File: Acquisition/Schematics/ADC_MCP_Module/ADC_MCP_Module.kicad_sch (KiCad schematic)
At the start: 35 parts, among them J1 Can, J2 AudioJack4_SwitchTR1, J3 Conn_02x06_Counter_Clockwise, Q1 IRLML9301, SW1 SW_DIP_x01

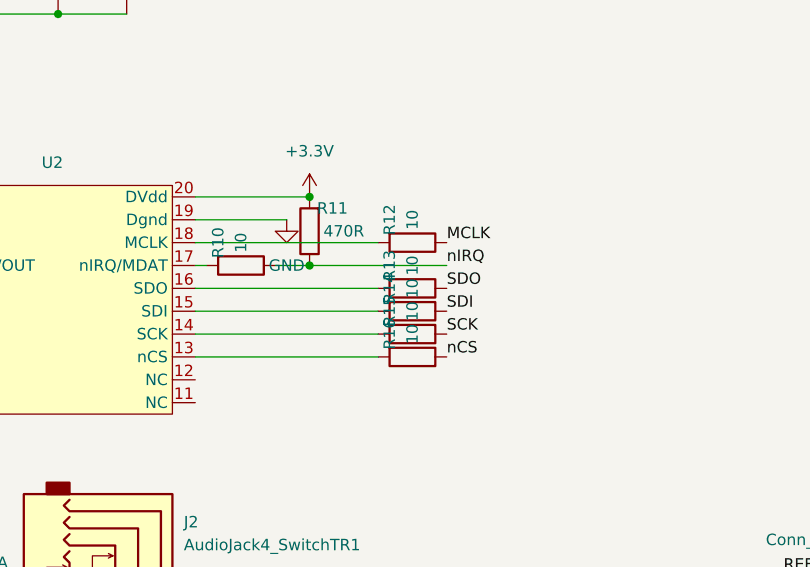
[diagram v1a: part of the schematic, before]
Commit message: ADC board prototype - ORDER
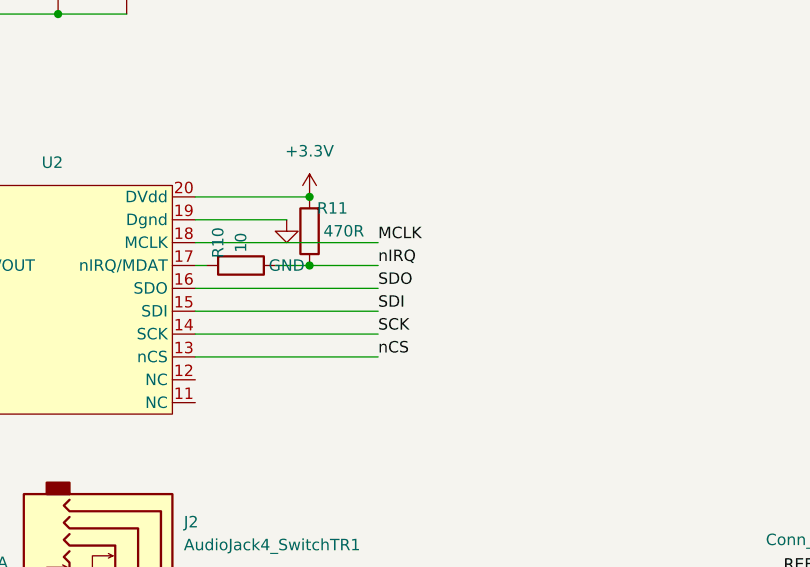
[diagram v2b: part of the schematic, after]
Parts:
- removed R12, R13, R14, R15, R16: 10, Resistor_SMD:R_0603_1608Metric, symbol Device:R
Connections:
- net MCLK: now also U2.18 (MCLK)
- net Out: now also U2.16 (SDO)
- net SCK: now also U2.14 (SCK)
- net SDI: now also U2.15 (SDI)
- net nCS: now also U2.13 (nCS)
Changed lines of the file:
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@@
     (stroke (width 0) (type default))
   )
-  (wire (pts (xy 144.78 57.15) (xy 160.02 57.15))
+  (wire (pts (xy 144.78 57.15) (xy 152.4 57.15))
     (stroke (width 0) (type default))
   )
@@
     (effects (font (size 1.27 1.27)) (justify left bottom))
   )
-  (label "nCS" (at 160.02 67.31 0) (fields_autoplaced)
-    (effects (font (size 1.27 1.27)) (justify left bottom))
-  )
-  (label "nIRQ" (at 160.02 57.15 0) (fields_autoplaced)
-    (effects (font (size 1.27 1.27)) (justify left bottom))
-  )
-  (label "SDO" (at 160.02 59.69 0) (fields_autoplaced)
+  (label "nCS" (at 152.4 67.31 0) (fields_autoplaced)
+    (effects (font (size 1.27 1.27)) (justify left bottom))
+  )
+  (label "nIRQ" (at 152.4 57.15 0) (fields_autoplaced)
+    (effects (font (size 1.27 1.27)) (justify left bottom))
+  )
+  (label "SDO" (at 152.4 59.69 0) (fields_autoplaced)
     (effects (font (size 1.27 1.27)) (justify left bottom))
   )
@@
     (effects (font (size 1.27 1.27)) (justify right bottom))
   )
-  (label "SDI" (at 160.02 62.23 0) (fields_autoplaced)
-    (effects (font (size 1.27 1.27)) (justify left bottom))
-  )
-  (label "MCLK" (at 160.02 54.61 0) (fields_autoplaced)
+  (label "SDI" (at 152.4 62.23 0) (fields_autoplaced)
+    (effects (font (size 1.27 1.27)) (justify left bottom))
+  )
+  (label "MCLK" (at 152.4 54.61 0) (fields_autoplaced)
     (effects (font (size 1.27 1.27)) (justify left bottom))
   )
@@
     (effects (font (size 1.27 1.27)) (justify right bottom))
   )
-  (label "SCK" (at 160.02 64.77 0) (fields_autoplaced)
+  (label "SCK" (at 152.4 64.77 0) (fields_autoplaced)
     (effects (font (size 1.27 1.27)) (justify left bottom))
   )
@@
     )
   )
-  (symbol (lib_id "Device:R") (at 156.21 62.23 270) (unit 1)
-    (in_bom yes) (on_board yes) (dnp no)
-    (property "Reference" "R14" (at 153.67 59.69 0)
-      (effects (font (size 1.27 1.27)))
-    )
-    (property "Value" "10" (at 156.21 59.69 0)
-      (effects (font (size 1.27 1.27)))
-    )
-    (property "Footprint" "Resistor_SMD:R_0603_1608Metric" (at 156.21 60.452 90)
-      (effects (font (size 1.27 1.27)) hide)
-    )
-    (property "Datasheet" "~" (at 156.21 62.23 0)
-      (effects (font (size 1.27 1.27)) hide)
-    )
-    (pin "2")
-    (pin "1")
-    (instances
-      (project "ADC_MCP_Module"
-        (path "/af487b5e-a3f1-4982-9322-f2a7f87ce403"
-          (reference "R14") (unit 1)
-        )
-      )
-    )
-  )
-  (symbol (lib_id "Device:R") (at 156.21 54.61 270) (unit 1)
-    (in_bom yes) (on_board yes) (dnp no)
-    (property "Reference" "R12" (at 153.67 52.07 0)
-      (effects (font (size 1.27 1.27)))
-    )
-    (property "Value" "10" (at 156.21 52.07 0)
-      (effects (font (size 1.27 1.27)))
-    )
-    (property "Footprint" "Resistor_SMD:R_0603_1608Metric" (at 156.21 52.832 90)
-      (effects (font (size 1.27 1.27)) hide)
-    )
-    (property "Datasheet" "~" (at 156.21 54.61 0)
-      (effects (font (size 1.27 1.27)) hide)
-    )
-    (pin "2")
-    (pin "1")
-    (instances
-      (project "ADC_MCP_Module"
-        (path "/af487b5e-a3f1-4982-9322-f2a7f87ce403"
-          (reference "R12") (unit 1)
-        )
-      )
-    )
-  )
   (symbol (lib_id "power:GND") (at 80.01 64.77 0) (unit 1)
     (in_bom yes) (on_board yes) (dnp no) (fields_autoplaced)
@@
     )
   )
-  (symbol (lib_id "Device:R") (at 156.21 64.77 270) (unit 1)
-    (in_bom yes) (on_board yes) (dnp no)
-    (property "Reference" "R15" (at 153.67 62.23 0)
-      (effects (font (size 1.27 1.27)))
-    )
-    (property "Value" "10" (at 156.21 62.23 0)
-      (effects (font (size 1.27 1.27)))
-    )
-    (property "Footprint" "Resistor_SMD:R_0603_1608Metric" (at 156.21 62.992 90)
-      (effects (font (size 1.27 1.27)) hide)
-    )
-    (property "Datasheet" "~" (at 156.21 64.77 0)
-      (effects (font (size 1.27 1.27)) hide)
-    )
-    (pin "2")
-    (pin "1")
-    (instances
-      (project "ADC_MCP_Module"
-        (path "/af487b5e-a3f1-4982-9322-f2a7f87ce403"
-          (reference "R15") (unit 1)
-        )
-      )
-    )
-  )
   (symbol (lib_id "Device:C") (at 171.45 104.14 0) (unit 1)
     (in_bom yes) (on_board yes) (dnp no) (fields_autoplaced)
@@
         (path "/af487b5e-a3f1-4982-9322-f2a7f87ce403"
           (reference "C3") (unit 1)
-        )
-      )
-    )
-  )
-  (symbol (lib_id "Device:R") (at 156.21 67.31 270) (unit 1)
-    (in_bom yes) (on_board yes) (dnp no)
-    (property "Reference" "R16" (at 153.67 64.77 0)
-      (effects (font (size 1.27 1.27)))
-    )
-    (property "Value" "10" (at 156.21 64.77 0)
-      (effects (font (size 1.27 1.27)))
-    )
-    (property "Footprint" "Resistor_SMD:R_0603_1608Metric" (at 156.21 65.532 90)
-      (effects (font (size 1.27 1.27)) hide)
-    )
-    (property "Datasheet" "~" (at 156.21 67.31 0)
-      (effects (font (size 1.27 1.27)) hide)
-    )
-    (pin "2")
-    (pin "1")
-    (instances
-      (project "ADC_MCP_Module"
-        (path "/af487b5e-a3f1-4982-9322-f2a7f87ce403"
-          (reference "R16") (unit 1)
         )
       )
@@
         )
       )
-    )
-  )
-  (symbol (lib_id "Device:R") (at 156.21 59.69 270) (unit 1)
-    (in_bom yes) (on_board yes) (dnp no)
-    (property "Reference" "R13" (at 153.67 57.15 0)
-      (effects (font (size 1.27 1.27)))
-    )
-    (property "Value" "10" (at 156.21 57.15 0)
-      (effects (font (size 1.27 1.27)))
-    )
-    (property "Footprint" "Resistor_SMD:R_0603_1608Metric" (at 156.21 57.912 90)
-      (effects (font (size 1.27 1.27)) hide)
-    )
-    (property "Datasheet" "~" (at 156.21 59.69 0)
-      (effects (font (size 1.27 1.27)) hide)
-    )
-    (pin "2")
-    (pin "1")
-    (instances
-      (project "ADC_MCP_Module"
-        (path "/af487b5e-a3f1-4982-9322-f2a7f87ce403"
-          (reference "R13") (unit 1)
-        )
-      )
